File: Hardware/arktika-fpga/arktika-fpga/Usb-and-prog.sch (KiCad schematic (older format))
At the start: 43 parts

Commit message: Misc changes and fixes
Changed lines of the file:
@@
 AR Path="/5F448A9D" Ref="#PWR?"  Part="1"
 AR Path="/5F3E98C5/5F448A9D" Ref="#PWR?"  Part="1"
-AR Path="/5F415705/5F448A9D" Ref="#PWR?"  Part="1"
-F 0 "#PWR?" H 9650 2450 50  0001 C CNN
+AR Path="/5F415705/5F448A9D" Ref="#PWR0116"  Part="1"
+F 0 "#PWR0116" H 9650 2450 50  0001 C CNN
 F 1 "GND" H 9650 2550 50  0000 C CNN
 F 2 "" H 9650 2700 50  0001 C CNN
@@
 AR Path="/5F448AC2" Ref="#PWR?"  Part="1"
 AR Path="/5F3E98C5/5F448AC2" Ref="#PWR?"  Part="1"
-AR Path="/5F415705/5F448AC2" Ref="#PWR?"  Part="1"
-F 0 "#PWR?" H 10650 2200 50  0001 C CNN
+AR Path="/5F415705/5F448AC2" Ref="#PWR0117"  Part="1"
+F 0 "#PWR0117" H 10650 2200 50  0001 C CNN
 F 1 "GND" H 10650 2300 50  0000 C CNN
 F 2 "" H 10650 2450 50  0001 C CNN
@@
 	1900 3800 2850 3800
 $Comp
-L power:GND #PWR?
+L power:GND #PWR0118
 U 1 1 5F4B6DED
 P 1900 5000
-F 0 "#PWR?" H 1900 4750 50  0001 C CNN
+F 0 "#PWR0118" H 1900 4750 50  0001 C CNN
 F 1 "GND" H 1905 4827 50  0000 C CNN
 F 2 "" H 1900 5000 50  0001 C CNN
@@
 $EndComp
 $Comp
-L power:GND #PWR?
+L power:GND #PWR0119
 U 1 1 5F4B8617
 P 1900 4100
-F 0 "#PWR?" H 1900 3850 50  0001 C CNN
+F 0 "#PWR0119" H 1900 3850 50  0001 C CNN
 F 1 "GND" H 1905 3927 50  0000 C CNN
 F 2 "" H 1900 4100 50  0001 C CNN
@@
 $EndComp
 $Comp
-L power:GND #PWR?
+L power:GND #PWR0120
 U 1 1 5F4B8C50
 P 1300 3450
-F 0 "#PWR?" H 1300 3200 50  0001 C CNN
+F 0 "#PWR0120" H 1300 3200 50  0001 C CNN
 F 1 "GND" H 1305 3277 50  0000 C CNN
 F 2 "" H 1300 3450 50  0001 C CNN
@@
 $EndComp
 $Comp
-L power:GND #PWR?
+L power:GND #PWR0121
 U 1 1 5F4B9767
 P 3000 1600
-F 0 "#PWR?" H 3000 1350 50  0001 C CNN
+F 0 "#PWR0121" H 3000 1350 50  0001 C CNN
 F 1 "GND" H 3005 1427 50  0000 C CNN
 F 2 "" H 3000 1600 50  0001 C CNN
@@
 $EndComp
 $Comp
-L power:GND #PWR?
+L power:GND #PWR0122
 U 1 1 5F4B9F55
 P 3400 1600
-F 0 "#PWR?" H 3400 1350 50  0001 C CNN
+F 0 "#PWR0122" H 3400 1350 50  0001 C CNN
 F 1 "GND" H 3405 1427 50  0000 C CNN
 F 2 "" H 3400 1600 50  0001 C CNN
@@
 $EndComp
 $Comp
-L power:GND #PWR?
+L power:GND #PWR0123
 U 1 1 5F4BA2D0
 P 3800 1600
-F 0 "#PWR?" H 3800 1350 50  0001 C CNN
+F 0 "#PWR0123" H 3800 1350 50  0001 C CNN
 F 1 "GND" H 3805 1427 50  0000 C CNN
 F 2 "" H 3800 1600 50  0001 C CNN
@@
 $EndComp
 $Comp
-L power:GND #PWR?
+L power:GND #PWR0124
 U 1 1 5F4BA61E
 P 4600 1650
-F 0 "#PWR?" H 4600 1400 50  0001 C CNN
+F 0 "#PWR0124" H 4600 1400 50  0001 C CNN
 F 1 "GND" H 4605 1477 50  0000 C CNN
 F 2 "" H 4600 1650 50  0001 C CNN
@@
 	4250 5400 4350 5400
 $Comp
-L power:GND #PWR?
+L power:GND #PWR0125
 U 1 1 5F4BCC98
 P 3850 5400
-F 0 "#PWR?" H 3850 5150 50  0001 C CNN
+F 0 "#PWR0125" H 3850 5150 50  0001 C CNN
 F 1 "GND" H 3855 5227 50  0000 C CNN
 F 2 "" H 3850 5400 50  0001 C CNN
@@
 AR Path="/5F53F910" Ref="#PWR?"  Part="1"
 AR Path="/5F3E98C5/5F53F910" Ref="#PWR?"  Part="1"
-AR Path="/5F415705/5F53F910" Ref="#PWR?"  Part="1"
-F 0 "#PWR?" H 9400 4800 50  0001 C CNN
+AR Path="/5F415705/5F53F910" Ref="#PWR0126"  Part="1"
+F 0 "#PWR0126" H 9400 4800 50  0001 C CNN
 F 1 "GND" H 9400 4900 50  0000 C CNN
 F 2 "" H 9400 5050 50  0001 C CNN
@@
 AR Path="/5F5CC008" Ref="#PWR?"  Part="1"
 AR Path="/5F3E98C5/5F5CC008" Ref="#PWR?"  Part="1"
-AR Path="/5F415705/5F5CC008" Ref="#PWR?"  Part="1"
-F 0 "#PWR?" H 9400 5850 50  0001 C CNN
+AR Path="/5F415705/5F5CC008" Ref="#PWR0127"  Part="1"
+F 0 "#PWR0127" H 9400 5850 50  0001 C CNN
 F 1 "GND" H 9400 5950 50  0000 C CNN
 F 2 "" H 9400 6100 50  0001 C CNN
@@
 	1500 4800 1500 5000
 $Comp
-L power:GND #PWR?
+L power:GND #PWR0128
 U 1 1 5F62F66B
 P 1750 4600
-F 0 "#PWR?" H 1750 4350 50  0001 C CNN
+F 0 "#PWR0128" H 1750 4350 50  0001 C CNN
 F 1 "GND" H 1755 4427 50  0000 C CNN
 F 2 "" H 1750 4600 50  0001 C CNN
@@
 $EndComp
 $Comp
-L power:GND #PWR?
+L power:GND #PWR0129
 U 1 1 5F630354
 P 1250 4600
-F 0 "#PWR?" H 1250 4350 50  0001 C CNN
+F 0 "#PWR0129" H 1250 4350 50  0001 C CNN
 F 1 "GND" H 1255 4427 50  0000 C CNN
 F 2 "" H 1250 4600 50  0001 C CNN
@@
 	1600 4600 1750 4600
 $Comp
-L power:GND #PWR?
+L power:GND #PWR0130
 U 1 1 5F640280
 P 1000 4200
-F 0 "#PWR?" H 1000 3950 50  0001 C CNN
+F 0 "#PWR0130" H 1000 3950 50  0001 C CNN
 F 1 "GND" H 1005 4027 50  0000 C CNN
 F 2 "" H 1000 4200 50  0001 C CNN
@@
 $EndComp
 $Comp
-L power:GND #PWR?
+L power:GND #PWR0131
 U 1 1 5F64094D
 P 1000 5000
-F 0 "#PWR?" H 1000 4750 50  0001 C CNN
+F 0 "#PWR0131" H 1000 4750 50  0001 C CNN
 F 1 "GND" H 1005 4827 50  0000 C CNN
 F 2 "" H 1000 5000 50  0001 C CNN
@@
 VCC3V3_USB
 $Comp
-L power:GND #PWR?
+L power:GND #PWR0132
 U 1 1 5F64F8ED
 P 1800 6750
-F 0 "#PWR?" H 1800 6500 50  0001 C CNN
+F 0 "#PWR0132" H 1800 6500 50  0001 C CNN
 F 1 "GND" H 1805 6577 50  0000 C CNN
 F 2 "" H 1800 6750 50  0001 C CNN
@@
 Wire Wire Line
 	1800 6700 1800 6750
+Text HLabel 950  7350 0    50   Input ~ 0
+GND
+$Comp
+L power:GND #PWR?
+U 1 1 5F2C0418
+P 1250 7350
+AR Path="/5F2C0418" Ref="#PWR?"  Part="1"
+AR Path="/5F3E98C5/5F2C0418" Ref="#PWR?"  Part="1"
+AR Path="/5F415705/5F2C0418" Ref="#PWR0133"  Part="1"
+F 0 "#PWR0133" H 1250 7100 50  0001 C CNN
+F 1 "GND" H 1250 7200 50  0000 C CNN
+F 2 "" H 1250 7350 50  0001 C CNN
+F 3 "" H 1250 7350 50  0001 C CNN
+	1    1250 7350
+	1    0    0    -1
+$EndComp
+Wire Wire Line
+	1250 7350 950  7350
 $EndSCHEMATC

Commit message: Addded new hybrid crystal footprint, fixed missing footprints, created layout file for testing
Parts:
- CUP1, CUP10, CUP2, CUP3, CUP4, CUP5, CUP6, CUP8_1, CUP8_2: footprint Capacitors_SMD:C_0603 -> Capacitors_SMD:C_0603_HandSoldering
- CUP7, CUP9: footprint (none) -> Capacitors_SMD:C_0603_HandSoldering
- DUP1, DUP2, DUP3: footprint (none) -> LEDs:LED_0603_HandSoldering
- JUP1, JUP2, JUP3, JUP4: footprint (none) -> Jumper:SolderJumper-2_P1.3mm_Open_RoundedPad1.0x1.5mm
- JUP5_1, JUP5_2: footprint (none) -> Jumper:SolderJumper-2_P1.3mm_Bridged2Bar_RoundedPad1.0x1.5mm
- JUP6: footprint (none) -> Pin_Headers:Pin_Header_Straight_1x18_Pitch2.54mm
- JUP7_1, JUP7_2: footprint (none) -> Pin_Headers:Pin_Header_Straight_1x08_Pitch2.54mm
- JUP8_1, JUP8_2: footprint (none) -> Pin_Headers:Pin_Header_Straight_1x02_Pitch2.54mm
- JUP9: footprint (none) -> Pin_Headers:Pin_Header_Straight_1x07_Pitch2.54mm
- RUP1, RUP2, RUP3, RUP4, RUP5, RUP6, RUP7, RUP8: footprint Resistors_SMD:R_0603 -> Resistors_SMD:R_0603_HandSoldering
- RUP7_1, RUP7_2, RUP7_3, RUP7_4: footprint (none) -> Resistors_SMD:R_0603_HandSoldering
- UUP1: footprint (none) -> Housings_QFP:LQFP-48_7x7mm_Pitch0.5mm
- UUP2: footprint Package_TO_SOT_SMD:SOT-23-6 -> TO_SOT_Packages_SMD:SOT-23-6_Handsoldering
- UUP3: renamed from UP3; footprint Package_QFP:TQFP-144_20x20mm_P0.5mm -> Housings_QFP:TQFP-144_20x20mm_Pitch0.5mm
- UUP4: footprint Package_SO:SOIC-8_5.23x5.23mm_P1.27mm -> Housings_SOIC:SOIC-8_3.9x4.9mm_Pitch1.27mm

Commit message: Misc schematic changes. Preliminary layout almost complete
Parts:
- CUP1, CUP10, CUP2, CUP3, CUP4, CUP5, CUP6, CUP7, CUP8_1, CUP8_2, CUP9: footprint Capacitors_SMD:C_0603_HandSoldering -> Capacitor_SMD:C_0603_1608Metric_Pad1.05x0.95mm_HandSolder; symbol Device:C -> arktika-fpga-rescue:C-Device
- DUP1, DUP2, DUP3: footprint LEDs:LED_0603_HandSoldering -> LED_SMD:LED_0603_1608Metric_Pad1.05x0.95mm_HandSolder; symbol Device:LED -> arktika-fpga-rescue:LED-Device
- JUP1, JUP2, JUP3, JUP4: symbol Jumper:SolderJumper_2_Open -> arktika-fpga-rescue:SolderJumper_2_Open-Jumper
- JUP5_1, JUP5_2: symbol Jumper:SolderJumper_2_Bridged -> arktika-fpga-rescue:SolderJumper_2_Bridged-Jumper
- JUP6: symbol Connector_Generic:Conn_01x18 -> arktika-fpga-rescue:Conn_01x18-Connector_Generic
- JUP7_1, JUP7_2: symbol Connector_Generic:Conn_01x08 -> arktika-fpga-rescue:Conn_01x08-Connector_Generic
- JUP8_1, JUP8_2: symbol Connector_Generic:Conn_01x02 -> arktika-fpga-rescue:Conn_01x02-Connector_Generic
- JUP9: footprint Pin_Headers:Pin_Header_Straight_1x07_Pitch2.54mm -> Connector_PinHeader_2.54mm:PinHeader_1x07_P2.54mm_Horizontal; symbol Connector_Generic:Conn_01x07 -> arktika-fpga-rescue:Conn_01x07-Connector_Generic
- RUP1, RUP2, RUP3, RUP4, RUP5, RUP6, RUP7, RUP7_1, RUP7_2, RUP7_3, RUP7_4, RUP8: footprint Resistors_SMD:R_0603_HandSoldering -> Resistor_SMD:R_0603_1608Metric_Pad1.05x0.95mm_HandSolder; symbol Device:R_US -> arktika-fpga-rescue:R_US-Device
- UUP1: footprint Housings_QFP:LQFP-48_7x7mm_Pitch0.5mm -> Package_QFP:LQFP-48-1EP_7x7mm_P0.5mm_EP3.6x3.6mm; symbol Interface_USB:FT232H -> arktika-fpga-rescue:FT232H-Interface_USB
- UUP2: footprint TO_SOT_Packages_SMD:SOT-23-6_Handsoldering -> Package_TO_SOT_SMD:SOT-23-6_Handsoldering; symbol Memory_EEPROM:93LCxxBxxOT -> arktika-fpga-rescue:93LCxxBxxOT-Memory_EEPROM
- UUP3: footprint Housings_QFP:TQFP-144_20x20mm_Pitch0.5mm -> Package_QFP:TQFP-144_20x20mm_P0.5mm; symbol FPGA_Lattice:ICE40HX4K-TQ144 -> arktika-fpga-rescue:ICE40HX4K-TQ144-FPGA_Lattice
- UUP4: footprint Housings_SOIC:SOIC-8_3.9x4.9mm_Pitch1.27mm -> Package_SO:SOIC-8_3.9x4.9mm_P1.27mm; symbol Memory_Flash:W25Q128JVS -> arktika-fpga-rescue:W25Q128JVS-Memory_Flash
- YUP1: footprint Crystals:Crystal_SMD_3225-4pin_3.2x2.5mm_HandSoldering -> Crystal:Crystal_SMD_3225-4Pin_3.2x2.5mm_HandSoldering; symbol Device:Crystal_GND24_Small -> arktika-fpga-rescue:Crystal_GND24_Small-Device
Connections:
- net C8: no longer DUP2.1 (K)
- net C9: no longer DUP1.1 (K)
- net FLASH_CS: now also JUP9.6 (Pin_6); no longer JUP9.1 (Pin_1)
- net FLASH_MISO: now also JUP9.3 (Pin_3); no longer JUP9.4 (Pin_4)
- net FLASH_MOSI: now also JUP9.4 (Pin_4); no longer JUP9.3 (Pin_3)
- net ICE_SCK: now also JUP9.5 (Pin_5); no longer JUP9.2 (Pin_2)
- net VCC3V3: now also CUP4.1, CUP6.1
- net flash_~RST: now also JUP9.1 (Pin_1); no longer JUP9.6 (Pin_6)
- net flash_~WP: now also JUP9.2 (Pin_2); no longer JUP9.5 (Pin_5)
- net C8': now reaches JUP6.17 (Pin_17), JUP7_1.7 (Pin_7), UUP1.32 (ACBUS8)
- net C8': now also DUP1.1 (K)
- net C9': now reaches JUP6.18 (Pin_18), JUP7_1.8 (Pin_8), UUP1.33 (ACBUS9)
- net C9': now also DUP2.1 (K)
- net D'-: now reaches JUP5_1.2 (B), UUP1.6 (DM)
- net D'+: now reaches JUP5_2.2 (B), UUP1.7 (DP)

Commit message: Major routing updates. Did work on silkscreen. Optimized io placing. Misc changes
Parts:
- removed JUP6: Conn_01x18, Pin_Headers:Pin_Header_Straight_1x18_Pitch2.54mm, symbol arktika-fpga-rescue:Conn_01x18-Connector_Generic
- added JUP6: Conn_02x10_Odd_Even, Connector_PinHeader_2.54mm:PinHeader_2x10_P2.54mm_Vertical, symbol Connector_Generic:Conn_02x10_Odd_Even
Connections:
- net labels added: ACBUS0, ACBUS1, ACBUS2, ACBUS3, ACBUS4, ACBUS5, ACBUS6, ACBUS7, ADBUS0, ADBUS1, ADBUS2, ADBUS3, ADBUS4, ADBUS5, ADBUS6, ADBUS7
- wire segments 221 -> 214
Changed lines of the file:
@@
 Wire Wire Line
 	8550 2350 9050 2350
-$Comp
-L arktika-fpga-rescue:Conn_01x18-Connector_Generic JUP6
-U 1 1 5F1FD944
-P 5550 3500
-F 0 "JUP6" H 5550 4400 50  0000 L CNN
-F 1 "Conn_01x18" H 5400 2500 50  0000 L CNN
-F 2 "Pin_Headers:Pin_Header_Straight_1x18_Pitch2.54mm" H 5550 3500 50  0001 C CNN
-F 3 "~" H 5550 3500 50  0001 C CNN
-	1    5550 3500
-	1    0    0    -1
-$EndComp
 Wire Wire Line
 	4650 3000 5350 3000
@@
 	5350 3200 4650 3200
 Wire Wire Line
-	5350 4500 5350 4400
-Wire Wire Line
-	4650 4500 5350 4500
-Wire Wire Line
-	5300 4400 5300 4300
-Wire Wire Line
-	4650 4400 5300 4400
-Wire Wire Line
 	4650 4300 5250 4300
-Wire Wire Line
-	5250 4300 5250 4200
-Wire Wire Line
-	5250 4200 5350 4200
-Wire Wire Line
-	4650 4200 5200 4200
-Wire Wire Line
-	5200 4200 5200 4100
-Wire Wire Line
-	5200 4100 5350 4100
-Wire Wire Line
-	4650 4100 5150 4100
-Wire Wire Line
-	5150 4100 5150 4000
-Wire Wire Line
-	5150 4000 5350 4000
-Wire Wire Line
-	4650 4000 5100 4000
-Wire Wire Line
-	5100 4000 5100 3900
-Wire Wire Line
-	5100 3900 5350 3900
-Wire Wire Line
-	4650 3900 5050 3900
-Wire Wire Line
-	5050 3900 5050 3800
-Wire Wire Line
-	5050 3800 5350 3800
-Wire Wire Line
-	4650 3800 5000 3800
-Wire Wire Line
-	5000 3800 5000 3700
-Wire Wire Line
-	5000 3700 5350 3700
-Wire Wire Line
-	4650 3700 4950 3700
-Wire Wire Line
-	4950 3700 4950 3600
-Wire Wire Line
-	4950 3600 5350 3600
-Wire Wire Line
-	4650 3600 4900 3600
-Wire Wire Line
-	4900 3600 4900 3500
-Wire Wire Line
-	4900 3500 5350 3500
 Text Notes 4950 2350 0    50   ~ 0
 Place shunt between connectors for normal operation\n
@@
 $EndComp
 Wire Wire Line
-	4650 2700 5350 2700
-Connection ~ 5350 2700
-Wire Wire Line
-	4650 2800 5350 2800
-Connection ~ 5350 2800
-Wire Wire Line
-	4650 2900 5350 2900
-Connection ~ 5350 2900
-Wire Wire Line
 	5650 3100 5650 3000
 Wire Wire Line
-	4650 3100 5350 3100
-Connection ~ 5350 3100
-Wire Wire Line
-	5350 3100 5650 3100
-Wire Wire Line
 	5700 3300 5700 3100
 Wire Wire Line
-	4650 3300 5350 3300
-Connection ~ 5350 3300
-Wire Wire Line
-	5350 3300 5700 3300
-Wire Wire Line
-	5350 2700 5950 2700
-Wire Wire Line
-	5350 2800 5950 2800
-Wire Wire Line
-	5350 2900 5950 2900
-Wire Wire Line
 	5650 3000 5950 3000
 Wire Wire Line
@@
 	5750 3200 5950 3200
 Wire Wire Line
-	4650 3400 5350 3400
-Connection ~ 5350 3400
-Wire Wire Line
-	5350 3400 5750 3400
-Wire Wire Line
-	5800 4300 5800 3300
-Wire Wire Line
 	5800 3300 5950 3300
 Wire Wire Line
-	5350 4400 5850 4400
-Wire Wire Line
-	5850 4400 5850 3400
-Wire Wire Line
 	5850 3400 5950 3400
-Connection ~ 5350 4400
 Wire Wire Line
 	1800 6650 1800 6700
 Wire Wire Line
 	1300 3400 1300 3450
-Wire Wire Line
-	5300 4300 5350 4300
-Connection ~ 5350 4300
-Wire Wire Line
-	5350 4300 5800 4300
 $Comp
 L arktika-fpga-rescue:93LCxxBxxOT-Memory_EEPROM UUP2
@@
 Wire Wire Line
 	1650 1900 1500 1900
+Wire Wire Line
+	4650 2700 5950 2700
+Wire Wire Line
+	4650 2800 5950 2800
+Wire Wire Line
+	4650 2900 5950 2900
+Wire Wire Line
+	4650 3100 5650 3100
+Wire Wire Line
+	4650 3300 5700 3300
+Wire Wire Line
+	4650 3400 5750 3400
+Text Label 5000 2700 0    50   ~ 0
+ADBUS0
+Text Label 5000 2800 0    50   ~ 0
+ADBUS1
+Text Label 5000 2900 0    50   ~ 0
+ADBUS2
+Text Label 5000 3000 0    50   ~ 0
+ADBUS3
+Text Label 5000 3100 0    50   ~ 0
+ADBUS4
+Text Label 5000 3200 0    50   ~ 0
+ADBUS5
+Text Label 5000 3300 0    50   ~ 0
+ADBUS6
+Text Label 5000 3400 0    50   ~ 0
+ADBUS7
+Text Label 6400 4050 0    50   ~ 0
+ADBUS0
+Text Label 6400 4150 0    50   ~ 0
+ADBUS1
+Text Label 6400 4250 0    50   ~ 0
+ADBUS2
+Text Label 6400 4350 0    50   ~ 0
+ADBUS3
+Text Label 6400 4450 0    50   ~ 0
+ADBUS4
+Text Label 6400 4550 0    50   ~ 0
+ADBUS5
+Text Label 6400 4650 0    50   ~ 0
+ADBUS6
+Text Label 6400 4750 0    50   ~ 0
+ADBUS7
+Text Label 5000 3700 0    50   ~ 0
+ACBUS1
+Text Label 5000 3600 0    50   ~ 0
+ACBUS0
+Wire Wire Line
+	4650 4500 5850 4500
+Wire Wire Line
+	5850 3400 5850 4500
+Wire Wire Line
+	4650 4400 5800 4400
+Wire Wire Line
+	5800 3300 5800 4400
+Wire Wire Line
+	4650 3600 5250 3600
+Wire Wire Line
+	4650 3700 5250 3700
+Wire Wire Line
+	4650 3800 5250 3800
+Wire Wire Line
+	4650 3900 5250 3900
+Wire Wire Line
+	4650 4000 5250 4000
+Wire Wire Line
+	4650 4100 5250 4100
+Wire Wire Line
+	4650 4200 5250 4200
+Text Label 5000 3800 0    50   ~ 0
+ACBUS2
+Text Label 5000 3900 0    50   ~ 0
+ACBUS3
+Text Label 5000 4000 0    50   ~ 0
+ACBUS4
+Text Label 5000 4100 0    50   ~ 0
+ACBUS5
+Text Label 5000 4200 0    50   ~ 0
+ACBUS6
+Text Label 5000 4300 0    50   ~ 0
+ACBUS7
+Wire Wire Line
+	7250 4750 7850 4750
+Text Label 7600 4150 0    50   ~ 0
+ACBUS1
+Text Label 7600 4050 0    50   ~ 0
+ACBUS0
+Wire Wire Line
+	7250 4050 7850 4050
+Wire Wire Line
+	7250 4150 7850 4150
+Wire Wire Line
+	7250 4250 7850 4250
+Wire Wire Line
+	7250 4350 7850 4350
+Wire Wire Line
+	7250 4450 7850 4450
+Wire Wire Line
+	7250 4550 7850 4550
+Wire Wire Line
+	7250 4650 7850 4650
+Text Label 7600 4250 0    50   ~ 0
+ACBUS2
+Text Label 7600 4350 0    50   ~ 0
+ACBUS3
+Text Label 7600 4450 0    50   ~ 0
+ACBUS4
+Text Label 7600 4550 0    50   ~ 0
+ACBUS5
+Text Label 7600 4650 0    50   ~ 0
+ACBUS6
+Text Label 7600 4750 0    50   ~ 0
+ACBUS7
+Wire Wire Line
+	6150 4750 6750 4750
+Wire Wire Line
+	6150 4150 6750 4150
+Wire Wire Line
+	6150 4250 6750 4250
+Wire Wire Line
+	6150 4350 6750 4350
+Wire Wire Line
+	6150 4450 6750 4450
+Wire Wire Line
+	6150 4550 6750 4550
+Wire Wire Line
+	6150 4650 6750 4650
+Wire Wire Line
+	6150 4050 6750 4050
+$Comp
+L Connector_Generic:Conn_02x10_Odd_Even JUP6
+U 1 1 603EF912
+P 6950 4450
+F 0 "JUP6" H 7000 5067 50  0000 C CNN
+F 1 "Conn_02x10_Odd_Even" H 7000 4976 50  0000 C CNN
+F 2 "Connector_PinHeader_2.54mm:PinHeader_2x10_P2.54mm_Vertical" H 6950 4450 50  0001 C CNN
+F 3 "~" H 6950 4450 50  0001 C CNN
+	1    6950 4450
+	1    0    0    -1
+$EndComp
+Text Label 6400 4850 0    50   ~ 0
+C8'
+Text Label 7600 4850 0    50   ~ 0
+C9'
+Wire Wire Line
+	7850 4850 7250 4850
+Wire Wire Line
+	6750 4850 6150 4850
+$Comp
+L arktika-fpga-rescue:GND-power #PWR?
+U 1 1 6042592D
+P 6150 4950
+AR Path="/6042592D" Ref="#PWR?"  Part="1"
+AR Path="/5F3E98C5/6042592D" Ref="#PWR?"  Part="1"
+AR Path="/5F415705/6042592D" Ref="#PWR0159"  Part="1"
+F 0 "#PWR0159" H 6150 4700 50  0001 C CNN
+F 1 "GND" H 6150 4800 50  0000 C CNN
+F 2 "" H 6150 4950 50  0001 C CNN
+F 3 "" H 6150 4950 50  0001 C CNN
+	1    6150 4950
+	1    0    0    -1
+$EndComp
+$Comp
+L arktika-fpga-rescue:GND-power #PWR?
+U 1 1 604263FB
+P 7850 4950
+AR Path="/604263FB" Ref="#PWR?"  Part="1"
+AR Path="/5F3E98C5/604263FB" Ref="#PWR?"  Part="1"
+AR Path="/5F415705/604263FB" Ref="#PWR0160"  Part="1"
+F 0 "#PWR0160" H 7850 4700 50  0001 C CNN
+F 1 "GND" H 7850 4800 50  0000 C CNN
+F 2 "" H 7850 4950 50  0001 C CNN
+F 3 "" H 7850 4950 50  0001 C CNN
+	1    7850 4950
+	1    0    0    -1
+$EndComp
+Wire Wire Line
+	7850 4950 7250 4950
+Wire Wire Line
+	6150 4950 6750 4950
 $EndSCHEMATC

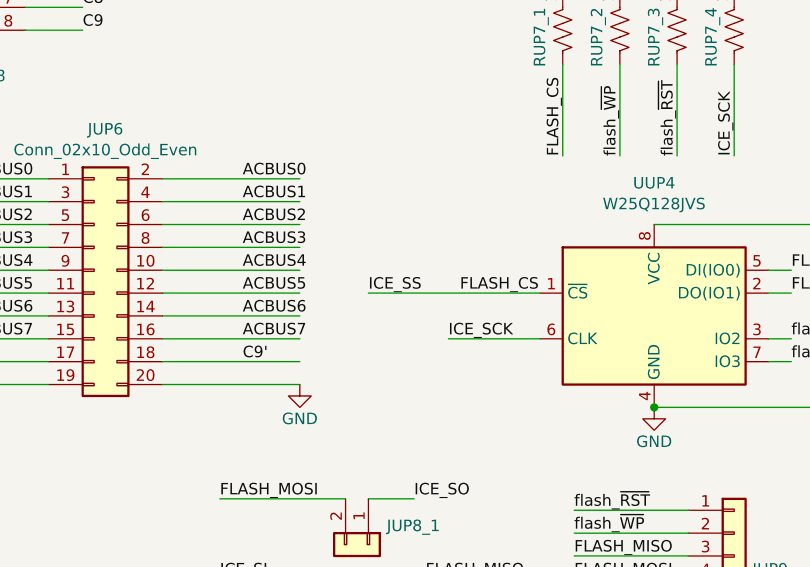
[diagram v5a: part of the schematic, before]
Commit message: Fixed flash CS net
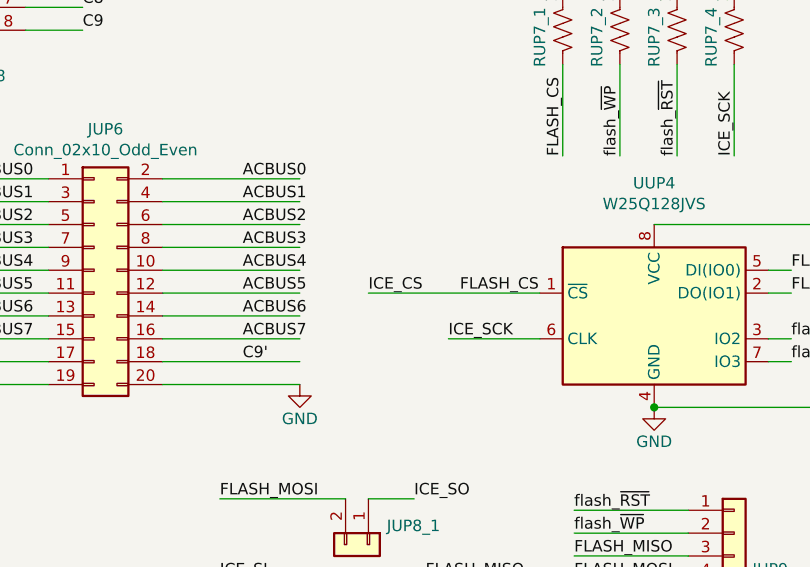
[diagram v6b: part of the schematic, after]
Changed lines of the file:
@@
 Wire Wire Line
 	9050 1850 8700 1850
-Text Label 8150 4550 0    50   ~ 0
-ICE_SS
 $Comp
 L arktika-fpga-rescue:GND-power #PWR?
@@
 Wire Wire Line
 	6150 4950 6750 4950
+Text Label 8150 4550 0    50   ~ 0
+ICE_CS
 $EndSCHEMATC
